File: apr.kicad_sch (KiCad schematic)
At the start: 46 parts, among them J1 EMATCH, J10 Screw_Terminal_01x02, J11 Screw_Terminal_01x02, J18 LORA, J2 BATERIA, J3 Screw_Terminal_01x02, J4 Screw_Terminal_01x02, J5 Screw_Terminal_01x02, J6 Conn_01x20_Pin, J7 Conn_01x20_Pin, J8 Screw_Terminal_01x02, J9 Screw_Terminal_01x02, Q1 TIP120, Q10 TIP120, Q11 TIP120, Q2 TIP120, Q3 TIP120, Q4 TIP120, Q5 TIP120, Q6 TIP120, Q8 TIP120

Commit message: Revisão e ajustes
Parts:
- added D9: 1N4001, Diode_THT:D_DO-41_SOD81_P10.16mm_Horizontal, symbol Diode:1N4001
- J18: footprint Connector_PinHeader_2.54mm:PinHeader_1x07_P2.54mm_Vertical -> Connector_PinSocket_2.54mm:PinSocket_1x07_P2.54mm_Vertical
- J6, J7: footprint Connector_PinHeader_2.54mm:PinHeader_1x20_P2.54mm_Vertical -> Connector_PinSocket_2.54mm:PinSocket_1x20_P2.54mm_Vertical
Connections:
- net +12V: now also D1.1 (K), D2.1 (K), D3.1 (K), D4.1 (K), D5.1 (K), D6.1 (K), D7.1 (K), D8.1 (K), D9.1 (K)
- net ARM: now also J6.9 (Pin_9); no longer J6.10 (Pin_10)
- net EMATCH: now also D8.2 (A); no longer D8.1 (K)
- net GND: now also J6.19 (Pin_19), D9.2 (A); no longer D1.2 (A), D2.2 (A), D3.2 (A), D4.2 (A), D5.2 (A), D6.2 (A), D7.2 (A), D8.2 (A), J6.2 (Pin_2)
- net IGNITE: now also J6.8 (Pin_8); no longer J6.9 (Pin_9)
- net INJECAO: now also J6.7 (Pin_7); no longer J6.8 (Pin_8)
- net INJECAO_PA7: now also D2.2 (A); no longer D2.1 (K)
- net LINHA: now also J6.14 (Pin_14); no longer J6.15 (Pin_15)
- net LINHA_ABASTECE: now also D3.2 (A); no longer D3.1 (K)
- net PURGALINHA: now also J6.12 (Pin_12); no longer J6.13 (Pin_13)
- net PURGATANQUE: now also J6.6 (Pin_6); no longer J6.7 (Pin_7)
- net PURGA_LINHA_PA2: now also D6.2 (A); no longer D6.1 (K)
- net PURGA_TANQUE_PB0: now also D4.2 (A); no longer D4.1 (K)
- net QUICK: now also J6.10 (Pin_10); no longer J6.11 (Pin_11)
- net QUICK_DISCONNECT_PA4: now also D7.2 (A); no longer D7.1 (K)
- net SUPER: now also J6.11 (Pin_11); no longer J6.12 (Pin_12)
- net SUPERCHARGE_PA3: now also D5.2 (A); no longer D5.1 (K)
- net VENT: now also J6.13 (Pin_13); no longer J6.14 (Pin_14)
- net VENT_PA1: now also D1.2 (A); no longer D1.1 (K)
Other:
- note added: "Blackpill Connection"
- note added: "LORA Connection"
- moved on the sheet: D1, D2, D3, D4, D5, D6, D7, D8, J18, J6, J7

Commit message: Ajustes finais
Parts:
- removed D9: 1N4001, Diode_THT:D_DO-41_SOD81_P10.16mm_Horizontal, symbol Diode:1N4001
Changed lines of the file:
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@@
 	)
 	(junction
-		(at 544.83 73.66)
-		(diameter 0)
-		(color 0 0 0 0)
-	)
-	(junction
-		(at 541.02 59.69)
-		(diameter 0)
-		(color 0 0 0 0)
-	)
-	(junction
 		(at 45.72 30.48)
 		(diameter 0)
@@
 	(wire
 		(pts
-			(xy 544.83 62.23) (xy 544.83 73.66)
+			(xy 544.83 62.23) (xy 544.83 74.93)
 		)
 		(stroke
@@
 	(wire
 		(pts
-			(xy 541.02 59.69) (xy 541.02 63.5)
-		)
-		(stroke
-			(width 0)
-			(type default)
-		)
-	)
-	(wire
-		(pts
 			(xy 77.47 110.49) (xy 77.47 96.52)
 		)
@@
 	(wire
 		(pts
-			(xy 537.21 59.69) (xy 541.02 59.69)
+			(xy 537.21 59.69) (xy 552.45 59.69)
 		)
 		(stroke
@@
 	(wire
 		(pts
-			(xy 544.83 73.66) (xy 544.83 74.93)
-		)
-		(stroke
-			(width 0)
-			(type default)
-		)
-	)
-	(wire
-		(pts
 			(xy 542.29 25.4) (xy 542.29 38.1)
 		)
@@
 	(wire
 		(pts
-			(xy 541.02 59.69) (xy 552.45 59.69)
-		)
-		(stroke
-			(width 0)
-			(type default)
-		)
-	)
-	(wire
-		(pts
 			(xy 41.91 115.57) (xy 41.91 120.65)
 		)
@@
 	(wire
 		(pts
-			(xy 541.02 73.66) (xy 544.83 73.66)
-		)
-		(stroke
-			(width 0)
-			(type default)
-		)
-	)
-	(wire
-		(pts
 			(xy 542.29 38.1) (xy 542.29 43.18)
 		)
@@
 	(wire
 		(pts
-			(xy 541.02 73.66) (xy 541.02 71.12)
-		)
-		(stroke
-			(width 0)
-			(type default)
-		)
-	)
-	(wire
-		(pts
 			(xy 541.02 121.92) (xy 554.99 121.92)
 		)
@@
 					(unit 1)
 				)
-			)
-		)
-	)
-	(symbol
-		(lib_id "Diode:1N4001")
-		(at 541.02 67.31 270)
-		(unit 1)
-		(exclude_from_sim no)
-		(in_bom yes)
-		(on_board yes)
-		(dnp no)
-		(property "Reference" "D9"
-			(at 538.48 68.5801 90)
-			(effects
-				(font
-					(size 1.27 1.27)
-				)
-				(justify right)
-			)
-		)
-		(property "Value" "1N4001"
-			(at 538.48 66.0401 90)
-			(effects
-				(font
-					(size 1.27 1.27)
-				)
-				(justify right)
-			)
-		)
-		(property "Footprint" "Diode_THT:D_DO-41_SOD81_P10.16mm_Horizontal"
-			(at 541.02 67.31 0)
-			(effects
-				(font
-					(size 1.27 1.27)
-				)
-				(hide yes)
-			)
-		)
-		(property "Datasheet" "http://www.vishay.com/docs/88503/1n4001.pdf"
-			(at 541.02 67.31 0)
-			(effects
-				(font
-					(size 1.27 1.27)
-				)
-				(hide yes)
-			)
-		)
-		(property "Description" "50V 1A General Purpose Rectifier Diode, DO-41"
-			(at 541.02 67.31 0)
-			(effects
-				(font
-					(size 1.27 1.27)
-				)
-				(hide yes)
-			)
-		)
-		(property "Sim.Device" "D"
-			(at 541.02 67.31 0)
-			(effects
-				(font
-					(size 1.27 1.27)
-				)
-				(hide yes)
-			)
-		)
-		(property "Sim.Pins" "1=K 2=A"
-			(at 541.02 67.31 0)
-			(effects
-				(font
-					(size 1.27 1.27)
-				)
-				(hide yes)
-			)
-		)
-		(pin "1"
-		)
-		(pin "2"
-		)
-		(instances
-			(project "apr"
-				(path "/2afdff1b-7fc0-44ff-9e54-bdf121523cb2"
-					(reference "D9")
-					(unit 1)
-				)

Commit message: Atualizações do dia 29_03
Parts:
- removed D1, D2, D3, D4, D5, D6, D7, D8: 1N4001, Diode_THT:D_DO-41_SOD81_P10.16mm_Horizontal, symbol Diode:1N4001
- removed J1: EMATCH, TerminalBlock:TerminalBlock_MaiXu_MX126-5.0-02P_1x02_P5.00mm, symbol Connector:Screw_Terminal_01x02
- removed J2: BATERIA, TerminalBlock:TerminalBlock_MaiXu_MX126-5.0-02P_1x02_P5.00mm, symbol Connector:Screw_Terminal_01x02
- removed Q1, Q10, Q11, Q2, Q3, Q4, Q5, Q6, Q8: TIP120, Package_TO_SOT_THT:TO-220-3_Vertical, symbol Transistor_BJT:TIP120
- removed R10, R3, R4, R6, R8: 100k, Resistor_THT:R_Axial_DIN0207_L6.3mm_D2.5mm_P15.24mm_Horizontal, symbol Device:R
- removed R11, R2, R5, R7, R9: 10k, Resistor_THT:R_Axial_DIN0207_L6.3mm_D2.5mm_P15.24mm_Horizontal, symbol Device:R
- added C1: C, Capacitor_THT:CP_Radial_D4.0mm_P1.50mm, symbol Device:C_Polarized
- added D1, D11, D12, D13, D14, D15, D16, D4, D8, D9: 1N4007, Diode_THT:D_DO-41_SOD81_P10.16mm_Horizontal, symbol Diode:1N4007
- added D10, D17, D18, D19, D20, D5, D6, D7: LED, symbol Device:LED
- added D2, D3: LED, LED_THT:LED_D5.0mm, symbol Device:LED
- added J1, J2, J30: Screw_Terminal_01x03, TerminalBlock:TerminalBlock_bornier-3_P5.08mm, symbol Connector:Screw_Terminal_01x03
- added J12, J20, J21, J22, J25, J26, J27, J28, J29: Screw_Terminal_01x02, TerminalBlock:TerminalBlock_bornier-2_P5.08mm, symbol Connector:Screw_Terminal_01x02
- added J13, J14: Conn_01x04, TerminalBlock:TerminalBlock_MaiXu_MX126-5.0-04P_1x04_P5.00mm, symbol Connector_Generic:Conn_01x04
- added J19: LORA, Connector_PinSocket_2.54mm:PinSocket_1x07_P2.54mm_Vertical, symbol Connector:Conn_01x07_Pin
- added J23, J24: Conn_01x20_Pin, Connector_PinSocket_2.54mm:PinSocket_1x20_P2.54mm_Vertical, symbol Connector:Conn_01x20_Pin
- added K1: Relay_SPDT, Relay_THT:Relay_SPDT_SANYOU_SRD_Series_Form_C, symbol Relay:Relay_SPDT
- added Q1: BC547, Package_TO_SOT_THT:TO-92_Inline, symbol Transistor_BJT:BC547
- added Q10, Q2, Q3, Q4, Q5, Q6, Q7, Q8, Q9: IRLZ34N, Package_TO_SOT_THT:TO-220-3_Vertical, symbol Transistor_FET:IRLZ34N
- added R16: 5.6k, Resistor_THT:R_Axial_DIN0207_L6.3mm_D2.5mm_P15.24mm_Horizontal, symbol Device:R
- added R17: 270k, Resistor_THT:R_Axial_DIN0207_L6.3mm_D2.5mm_P15.24mm_Horizontal, symbol Device:R
- added R22: 390k, Resistor_THT:R_Axial_DIN0207_L6.3mm_D2.5mm_P15.24mm_Horizontal, symbol Device:R
- added R23, R24: 470, Resistor_THT:R_Axial_DIN0207_L6.3mm_D2.5mm_P15.24mm_Horizontal, symbol Device:R
- added R25: 2k, symbol Device:R
- added R26, R27, R28, R29, R30, R31: 470, symbol Device:R
- added R32, R33, R34, R35: 4K7, Resistor_THT:R_Axial_DIN0207_L6.3mm_D2.5mm_P15.24mm_Horizontal, symbol Device:R
- added U1, U2: ~, Library:hx711, symbol Library:HX711
- added U3: LM7905_TO220, Package_TO_SOT_THT:TO-220-3_Vertical, symbol Regulator_Linear:LM7905_TO220
- J10, J11, J3, J4, J5, J8, J9: footprint TerminalBlock:TerminalBlock_MaiXu_MX126-5.0-02P_1x02_P5.00mm -> TerminalBlock:TerminalBlock_bornier-2_P5.08mm
- R1, R15: value 10k -> 470; footprint Resistor_THT:R_Axial_DIN0207_L6.3mm_D2.5mm_P15.24mm_Horizontal -> (none)
- R14, R18, R20: value 100k -> 4K7
- R19, R21: value 10k -> 4K7
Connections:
- net LINHA is gone; now on net VENT_PA1: J6.14 (Pin_14)
- net PURGALINHA is gone; now on net SUPER_CHARGE_PA3: J6.12 (Pin_12)
- net PURGA_LINHA_PA2 is gone; now on net PURGE_LINE: J3.2 (Pin_2)
- net SUPER is gone; now on net QUICK_DISCONNECT_PA4: J6.11 (Pin_11)
- net +12V: now also D1.1 (K), D11.1 (K), D12.1 (K), D13.1 (K), D14.1 (K), D15.1 (K), D16.1 (K), D4.1 (K), D8.1 (K), D9.1 (K), J1.1 (Pin_1), J12.1 (Pin_1), J2.1 (Pin_1), J25.2 (Pin_2), J26.1 (Pin_1), J27.2 (Pin_2), J28.2 (Pin_2), J30.1 (Pin_1), K1.A1
- net +3V3: now also D3.2 (A), J23.1 (Pin_1); no longer J18.6 (Pin_6)
- net ARM: now also D9.2 (A), J12.2 (Pin_2), Q7.2 (D), R27.2; no longer J6.9 (Pin_9), R1.1
- net GND: now also J6.2 (Pin_2), R19.1, R21.1, C1.2, J1.3 (Pin_3), J19.7 (Pin_7), J2.3 (Pin_3), J23.2 (Pin_2), J24.2 (Pin_2), J25.1 (Pin_1), J27.1 (Pin_1), J28.1 (Pin_1), J29.1 (Pin_1), J30.3 (Pin_3), Q1.3 (E), Q10.3 (S), Q2.3 (S), Q3.3 (S), Q4.3 (S), Q5.3 (S), Q6.3 (S), Q7.3 (S), Q8.3 (S), Q9.3 (S), R16.1, R17.1, R22.1, R23.1, R24.1, R32.1, R33.1, R34.1, R35.1, U1.10 (GND), U2.10 (GND), U3.1 (GND); no longer J6.19 (Pin_19)
- net IGNITE: now also D1.2 (A), J26.2 (Pin_2), Q10.2 (D); no longer J6.8 (Pin_8)
- net QUICK_DISCONNECT_PA4: now also R14.2, Q2.1 (G); no longer J5.2 (Pin_2)
- net VENT: now also J10.2 (Pin_2), D15.2 (A), Q8.2 (D), R26.2; no longer J6.13 (Pin_13)
- net VENT_PA1: now also R20.2, Q8.1 (G); no longer J10.2 (Pin_2)
- net SUPER_CHARGE_PA3: now reaches R19.2
- net SUPER_CHARGE_PA3: now also Q4.1 (G)
- net PURGE_LINE: now reaches R1.2
- net PURGE_LINE: now also R15.2, D13.2 (A), Q3.2 (D)
- net AUX_PB10: now reaches J18.5 (Pin_5)
- net AUX_PB10: now also J6.4 (Pin_4)
- net FUEL_LINE_A0: now reaches R21.2
- net FUEL_LINE_A0: now also J6.15 (Pin_15), Q9.1 (G)
- net RESET_PB2: now reaches J6.5 (Pin_5)
- net RESET_PB2: now also J24.16 (Pin_16)
- net M1_PA12: now reaches J7.12 (Pin_12)
- net M1_PA12: now also J18.2 (Pin_2)
- net M0_PA11: now reaches J7.13 (Pin_13)
- net M0_PA11: now also J18.1 (Pin_1)
- net +5V: now reaches J7.3 (Pin_3)
- net +5V: now also J18.6 (Pin_6), C1.1, D10.2 (A), D17.2 (A), D18.2 (A), D19.2 (A), D2.2 (A), D20.2 (A), D5.2 (A), D6.2 (A), D7.2 (A), J19.6 (Pin_6), J23.3 (Pin_3), U1.7 (VDD), U2.7 (VDD), U3.3 (VO)
- removed net INJECAO: J6.7 (Pin_7), R18.2, R19.1
- net INJECAO_PA7 renamed INJECTION
- net INJECTION: now also D16.2 (A), Q6.2 (D), R28.2
- net LINHA_ABASTECE renamed FUEL_LINE
- net FUEL_LINE: now also D14.2 (A), Q9.2 (D), R29.2
- net M0: no longer names the net of J7.17 (Pin_17)
- net M0: no longer J18.1 (Pin_1)
- net M1: no longer names the net of J7.16 (Pin_16)
- net M1: no longer J18.2 (Pin_2)
- removed net PURGATANQUE: J6.6 (Pin_6), R20.2, R21.1
- net PURGA_TANQUE_PB0 renamed PURGE_TANK
- net PURGE_TANK: now also D11.2 (A), Q5.2 (D), R30.2
- removed net QUICK: J6.10 (Pin_10), R14.2, R15.1
- net RX renamed RX1_PA10
- net RX1_PA10: now also J18.4 (Pin_4); no longer J18.3 (Pin_3)
- net SUPERCHARGE_PA3 renamed SUPER_CHARGE
- net SUPER_CHARGE: now also D8.2 (A), Q4.2 (D)
- net TX renamed TX1_PA9
- net TX1_PA9: now also J18.3 (Pin_3); no longer J18.4 (Pin_4)
- new net: J29.2 (Pin_2), U3.2 (VI)
- new net: D18.1 (K), R29.1
- new net: J13.4 (Pin_4), U2.1 (E+)
- new net: J13.3 (Pin_3), U2.2 (E-)
- new net: J13.2 (Pin_2), U2.3 (A-)
- new net: J13.1 (Pin_1), U2.4 (A+)
- new net: J14.1 (Pin_1), U1.4 (A+)
- new net: J14.2 (Pin_2), U1.3 (A-)
- new net: J14.3 (Pin_3), U1.2 (E-)
- new net: J14.4 (Pin_4), U1.1 (E+)
- new net: D10.1 (K), R27.1
- new net: D5.1 (K), R1.1
- new net: D3.1 (K), R24.2
- new net: D17.1 (K), R28.1
- new net: D19.1 (K), R30.1
- new net: D2.1 (K), R23.2
- new net: D4.2 (A), K1.A2, Q1.1 (C)
- new net: D7.1 (K), R26.1
- new net: D20.1 (K), R31.1
- new net: D6.1 (K), R15.1
- new net: Q1.2 (B), R25.2
- new net +3.3V: J20.1 (Pin_1), J21.1 (Pin_1), J22.1 (Pin_1)
- new net ARM_PA5: J6.10 (Pin_10), Q7.1 (G), R25.1, R34.2
- new net AUX_PB1: J19.5 (Pin_5), J24.6 (Pin_6)
- new net CS_PA8: J23.16 (Pin_16)
- new net DT1: J23.9 (Pin_9), U2.9 (DT)
- new net DT2: J23.7 (Pin_7), U1.9 (DT)
- new net IGNITE_PA6: J6.9 (Pin_9), Q10.1 (G), R35.2
- new net INJECTION_PA7: J6.8 (Pin_8), Q6.1 (G), R33.2
- new net M0_B12: J23.20 (Pin_20)
- new net M0_PB12: J19.1 (Pin_1)
- new net M1_B13: J23.19 (Pin_19)
- new net M1_PB13: J19.2 (Pin_2)
- new net MISO_PA15: J23.11 (Pin_11)
- new net MOSI_PA12: J23.12 (Pin_12)
- new net PURGE_LINE_PA2: J6.13 (Pin_13), Q3.1 (G), R18.2
- new net PURGE_TANK_PB0: J6.7 (Pin_7), Q5.1 (G), R32.2
- new net QUICK_DISCONNECT: D12.2 (A), J5.2 (Pin_2), Q2.2 (D), R31.2
- new net RX2_PA10: J19.4 (Pin_4), J23.14 (Pin_14)
- new net SAVE_PB1: J23.6 (Pin_6), J6.6 (Pin_6)
- new net SCK1: J23.10 (Pin_10), U2.8 (SCK)
- new net SCK2: J23.8 (Pin_8), U1.8 (SCK)
- new net SCK_PA11: J23.13 (Pin_13)
- new net THERMISTOR_CAMARA: J20.2 (Pin_2), J24.10 (Pin_10), R16.2
- new net THERMISTOR_LINE: J22.2 (Pin_2), J24.11 (Pin_11), R22.2
- new net THERMISTOR_TANK: J21.2 (Pin_2), J24.12 (Pin_12), R17.2
- new net TRANSDUCER_CAMARA_PA0: J24.15 (Pin_15), J30.2 (Pin_2)
- new net TRANSDUCER_LINE_PA2: J1.2 (Pin_2), J24.13 (Pin_13)
- new net TRANSDUCER_TANK_PA1: J2.2 (Pin_2), J24.14 (Pin_14)
- new net TX2_PA9: J19.3 (Pin_3), J23.15 (Pin_15)
- no-connect marks 25 -> 39
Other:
- note added: "."
- note added: "A+1"
- note added: "A+2"
- note added: "A-1"
- note added: "A-2"
- note added: "ARM"
- note added: "BLACKPILL CONNECTION ACTUATOR"
- note added: "BLACKPILL CONNECTION TRANSMISSION"
- note added: "BUSER"
- note added: "E+1"
- note added: "E+2"
- note added: "E-1"
- note added: "E-2"
- note added: "IGNITE"
- note added: "LOAD CELL 10 Hz"
- note added: "LOAD CELL 80 Hz"
- note added: "LORA CONNECTION E220"
- note added: "LORA CONNECTION E32"
- note added: "THERMISTOR CAMARA"
- note added: "THERMISTOR LINE"
- note added: "THERMISTOR TANK"
- note added: "VALVE: INJECTION"
- note added: "VALVE: LINE"
- note added: "VALVE: PURGE LINE"
- note added: "VALVE: PURGE TANK"
- note added: "VALVE: QUICK DISCONNECT"
- note added: "VALVE: SUPERCHARGE"
- note added: "VALVE: VENT"
- note added: "VALVES"
- note added: "VOLTAGE REGULATOR"
- note added: "VSUPPLY: AMPERE SENSOR 1"
- note added: "VSUPPLY: AMPERE SENSOR 2"
- note added: "VSUPPLY: AMPERE SENSOR 3"
- note added: "VSUPPLY: PRESSURE TRANSDUCER CAMARA"
- note added: "VSUPPLY: PRESSURE TRANSDUCER LINE"
- note added: "VSUPPLY: PRESSURE TRANSDUCER TANK"
- note removed: "Blackpill Connection"
- note removed: "LORA Connection"
- note removed: "VALVULA DISCONNECT"
- note removed: "VALVULA INJECAO"
- note removed: "VALVULA LINHA"
- note removed: "VALVULA PURGA LINHA"
- note removed: "VALVULA PURGA TANQUE"
- note removed: "VALVULA SUPERCHARGE"
- note removed: "VALVULA VENT"
- note removed: "VALVULAS"
- moved on the sheet: J10, J11, J18, J3, J4, J5, J6, J7, J8, J9, R14

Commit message: Troca do diodo para UF4007
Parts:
- removed D11, D12, D13, D14, D15, D16, D8, D9: 1N4007, Diode_THT:D_DO-41_SOD81_P10.16mm_Horizontal, symbol Diode:1N4007
- added CR1, CR2, CR3, CR4, CR5, CR6, CR7, CR8: UF4007-E3/73, DO-204AL_VIS, symbol Diode UF4007:UF4007-E3_73
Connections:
- net +12V: now also CR1.1, CR2.1, CR3.1, CR4.1, CR5.1, CR6.1, CR7.1, CR8.1
- net ARM: now also CR8.2
- net FUEL_LINE: now also CR5.2
- net INJECTION: now also CR7.2
- net PURGE_LINE: now also CR2.2
- net PURGE_TANK: now also CR3.2
- net QUICK_DISCONNECT: now also CR1.2
- net SUPER_CHARGE: now also CR4.2
- net VENT: now also CR6.2
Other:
- note added: "BUZZER RELAY"
- note removed: "BUSER"
- moved on the sheet: D5, D6, Q3, Q4, R1, R15, R18, R19

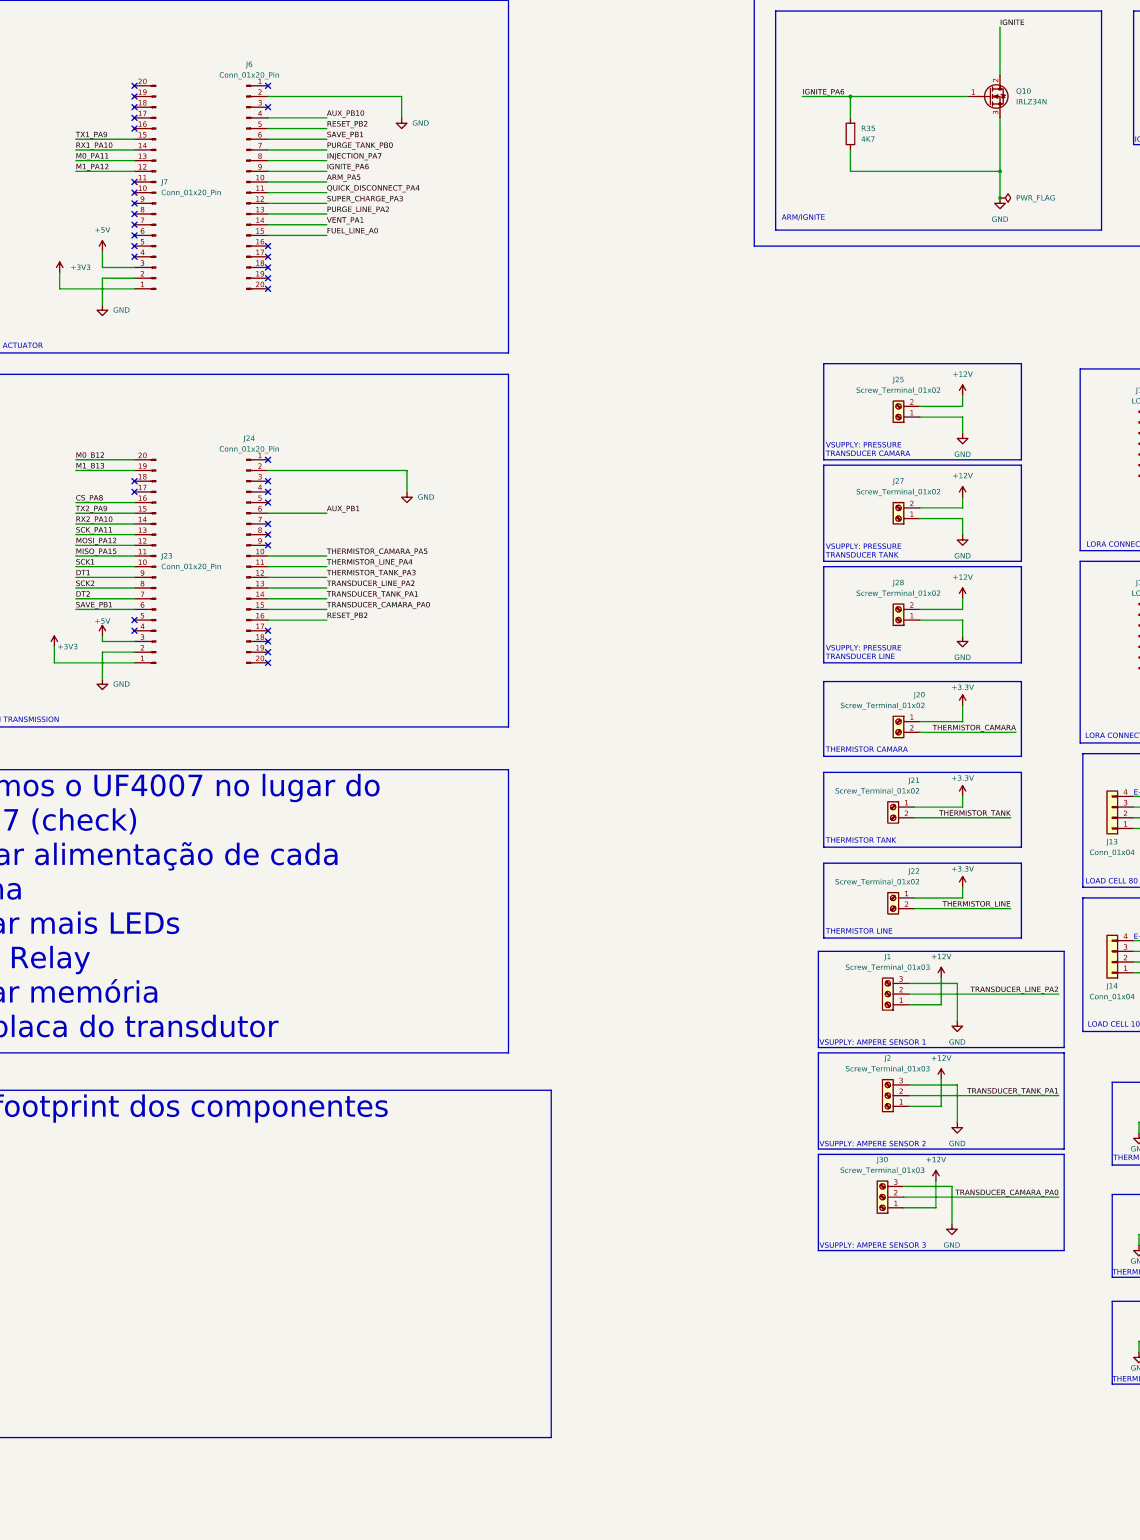
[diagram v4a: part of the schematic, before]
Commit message: Adiciona Flash no esquemático
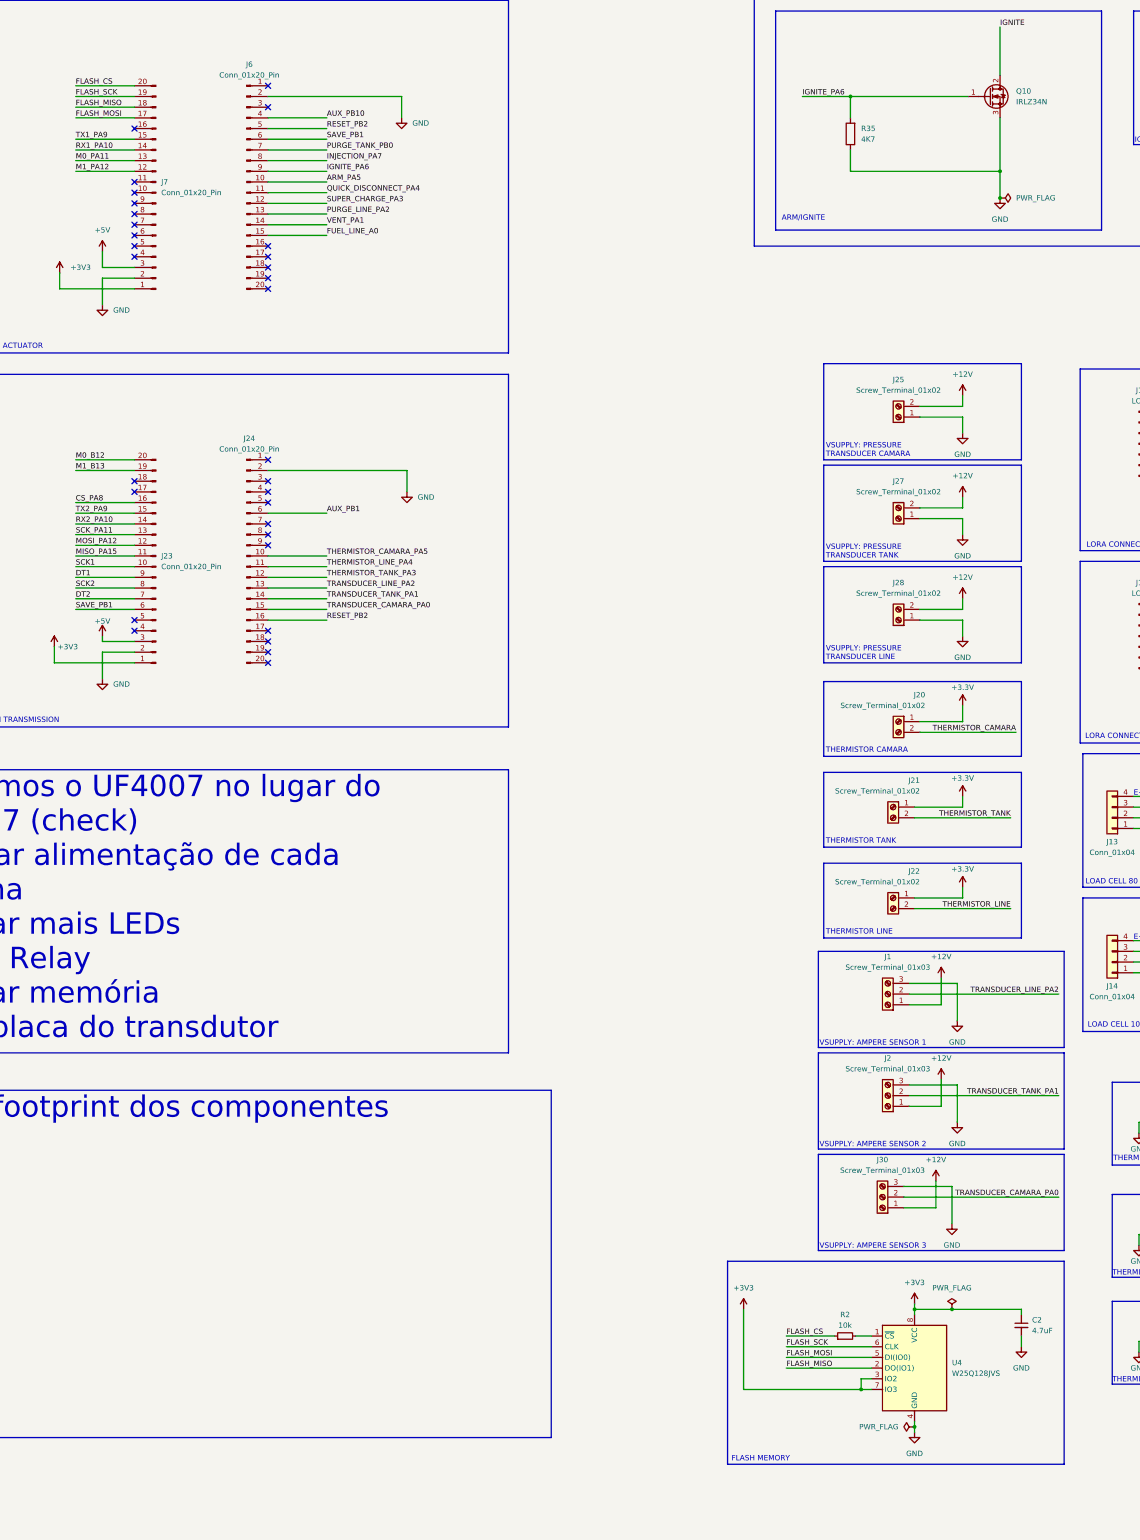
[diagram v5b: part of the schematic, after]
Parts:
- added C2: 4.7uF, Capacitor_SMD:C_0805_2012Metric, symbol Device:C_Small
- added R2: 10k, Resistor_SMD:R_0805_2012Metric, symbol Device:R_Small
- added U4: W25Q128JVS, Package_SO:SOIC-8_5.23x5.23mm_P1.27mm, symbol Memory_Flash:W25Q128JVS
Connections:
- net +3V3: now also C2.1, U4.3 (IO2), U4.7 (IO3), U4.8 (VCC)
- net GND: now also C2.2, U4.4 (GND)
- net FLASH_MOSI: now reaches J7.17 (Pin_17)
- net FLASH_MOSI: now also U4.5 (DI(IO0))
- net FLASH_MISO: now reaches J7.18 (Pin_18)
- net FLASH_MISO: now also U4.2 (DO(IO1))
- net FLASH_SCK: now reaches J7.19 (Pin_19)
- net FLASH_SCK: now also U4.6 (CLK)
- net FLASH_CS: now reaches J7.20 (Pin_20)
- net FLASH_CS: now also R2.1
- new net: R2.2, U4.1 (~{CS})
- no-connect marks 39 -> 35
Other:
- note added: "FLASH MEMORY"

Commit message: Separação das alimentações
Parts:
- removed J29: Screw_Terminal_01x02, TerminalBlock:TerminalBlock_bornier-2_P5.08mm, symbol Connector:Screw_Terminal_01x02
- added J15: Flash Module Conn, symbol Connector:Conn_01x06_Socket
- added J16: Bateria Lítio 1, Library:Screw Terminal 3D, symbol Connector:Screw_Terminal_01x02
- added J17: Bateria Lítio 2, Library:Screw Terminal 3D, symbol Connector:Screw_Terminal_01x02
- added J31: Bateria Lítio 3, Library:Screw Terminal 3D, symbol Connector:Screw_Terminal_01x02
- added J32: Buzzer, TerminalBlock:TerminalBlock_bornier-2_P5.08mm, symbol Connector:Screw_Terminal_01x02
- added J33: Bateria Lipo, symbol Connector:Conn_01x02_Pin
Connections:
- net +12V: now also J31.2 (Pin_2), J32.1 (Pin_1); no longer CR1.1, CR2.1, CR3.1, CR4.1, CR5.1, CR6.1, CR7.1, D1.1 (K), J10.1 (Pin_1), J11.1 (Pin_1), J26.1 (Pin_1), J3.1 (Pin_1), J4.1 (Pin_1), J5.1 (Pin_1), J8.1 (Pin_1), J9.1 (Pin_1)
- net +3V3: now also J15.1 (Pin_1)
- net FLASH_CS: now also J15.2 (Pin_2)
- net FLASH_MISO: now also J15.3 (Pin_3)
- net FLASH_MOSI: now also J15.6 (Pin_6)
- net FLASH_SCK: now also J15.5 (Pin_5)
- net GND: now also J15.4 (Pin_4), J16.1 (Pin_1), J17.1 (Pin_1), J31.1 (Pin_1), J33.2 (Pin_2)
- net at U3.2 (VI): now also J33.1 (Pin_1)
- net at D4.2 (A), K1.A2, Q1.1 (C): now also K1.11
- net at K1.14: now also J32.2 (Pin_2)
- new net +12C: CR1.1, CR6.1, D1.1 (K), J10.1 (Pin_1), J16.2 (Pin_2), J26.1 (Pin_1), J5.1 (Pin_1)
- new net +12L: CR2.1, CR3.1, CR4.1, CR5.1, CR7.1, J11.1 (Pin_1), J17.2 (Pin_2), J3.1 (Pin_1), J4.1 (Pin_1), J8.1 (Pin_1), J9.1 (Pin_1)
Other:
- note removed: "."
- moved on the sheet: C2, D1, D3, D4, J1, J13, J14, J18, J19, J2, J20, J21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
